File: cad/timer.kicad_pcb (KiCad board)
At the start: 2 copper layers, 47 x 47 mm, 22 parts, among them J1 Motor, J2 Pot, J4 Prog, Q1 S9012, Q2 S9013, Q3 S9012, U1 ATMEGA328P-PU, U2 LM393, U3 L293D, Y1 32.768kHz

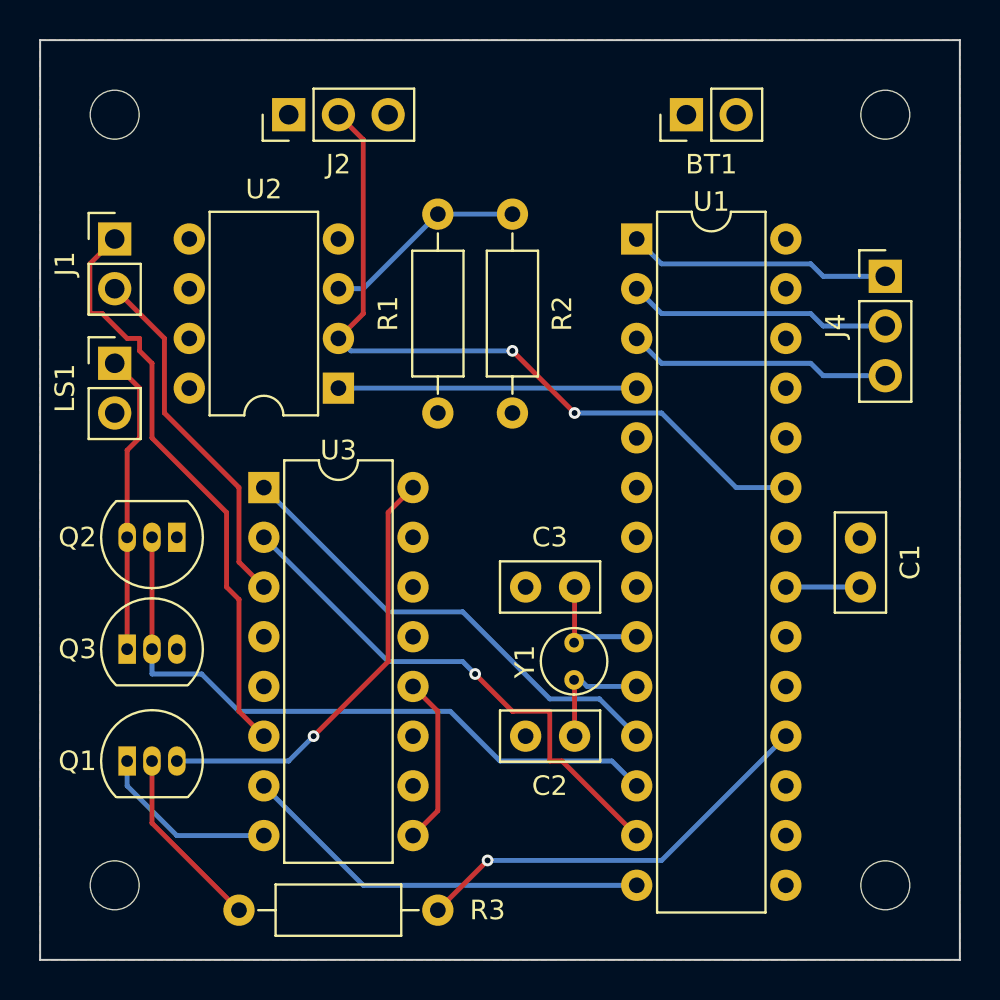
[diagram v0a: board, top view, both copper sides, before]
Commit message: Updated schematic and PCB design
- Increased hole size to 3mm
- Removed motor controller on/off switch (Q1 and R3)
- Swap transistor footprint for one that's easier to solder
- Reroute with FreeRoutingNew
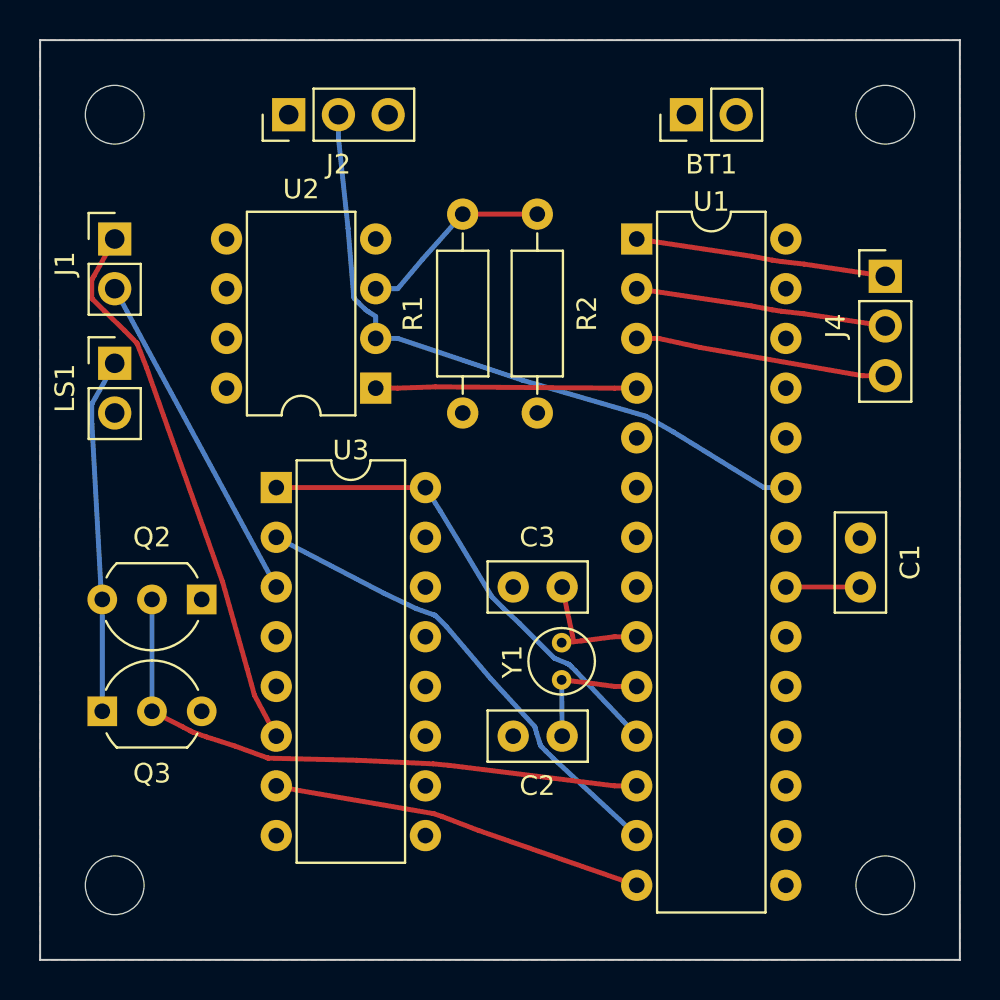
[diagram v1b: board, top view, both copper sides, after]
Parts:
- removed Q1: S9012, TO_SOT_Packages_THT:TO-92_Inline_Narrow_Oval
- removed R3: 10kΩ, Resistors_THT:R_Axial_DIN0207_L6.3mm_D2.5mm_P10.16mm_Horizontal
- H1, H2, H3, H4: value MountingHole_2.5mm -> MountingHole_3mm; footprint Mounting_Holes:MountingHole_2.5mm -> Mounting_Holes:MountingHole_3mm
- Q2, Q3: footprint TO_SOT_Packages_THT:TO-92_Inline_Narrow_Oval -> TO_SOT_Packages_THT:TO-92_Inline_Wide
- moved Q2 3.42 mm to (130.2, 97.8)
- moved Q3 3.42 mm to (125.1, 103.5)
- moved U2 1.91 mm to (139.1, 87.0)
- moved R1 1.27 mm to (143.5, 78.1)
- moved R2 1.27 mm to (147.3, 78.1)
- moved U3 0.64 mm to (134.0, 92.1)
- moved C2 0.63 mm to (148.6, 104.8)
- moved C3 0.63 mm to (148.6, 97.2)
- moved Y1 0.63 mm to (148.6, 101.9)
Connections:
- U3 pad 16: Net-(Q1-Pad3) -> Net-(U1-Pad11)
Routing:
- net Net-(Q1-Pad3): track 22.3 -> 0.00 mm, vias 1 -> 0
- net Net-(U1-Pad18): track 21.5 -> 0.00 mm, vias 1 -> 0
- net Net-(Q1-Pad2): track 9.46 -> 0.00 mm
- net VCC: track 9.31 -> 0.00 mm
- net GND: track 8.67 -> 0.00 mm
- net Net-(J2-Pad2): track 38.5 -> 34.6 mm, vias 2 -> 0
- net Net-(LS1-Pad1): track 15.4 -> 18.8 mm
- net Net-(Q2-Pad2): track 34.1 -> 31.0 mm
- net Net-(J1-Pad1): track 30.4 -> 27.9 mm
- net Net-(U1-Pad13): track 26.9 -> 24.4 mm, vias 1 -> 0
- net Net-(U1-Pad14): track 21.2 -> 19.2 mm
- net Net-(U1-Pad4): track 15.2 -> 13.3 mm
- net Net-(J1-Pad2): track 18.4 -> 17.3 mm
- net Net-(J4-Pad1): track 13.5 -> 12.8 mm
- net Net-(J4-Pad2): track 13.5 -> 12.8 mm
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
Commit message: New PCB design to match new schematic
- Isolated power networks with decoupling capacitors
- Top layer is ground, bottom layer is VCC (this seems to be the
  convention)
- Hopefully better placement of ports for external devices
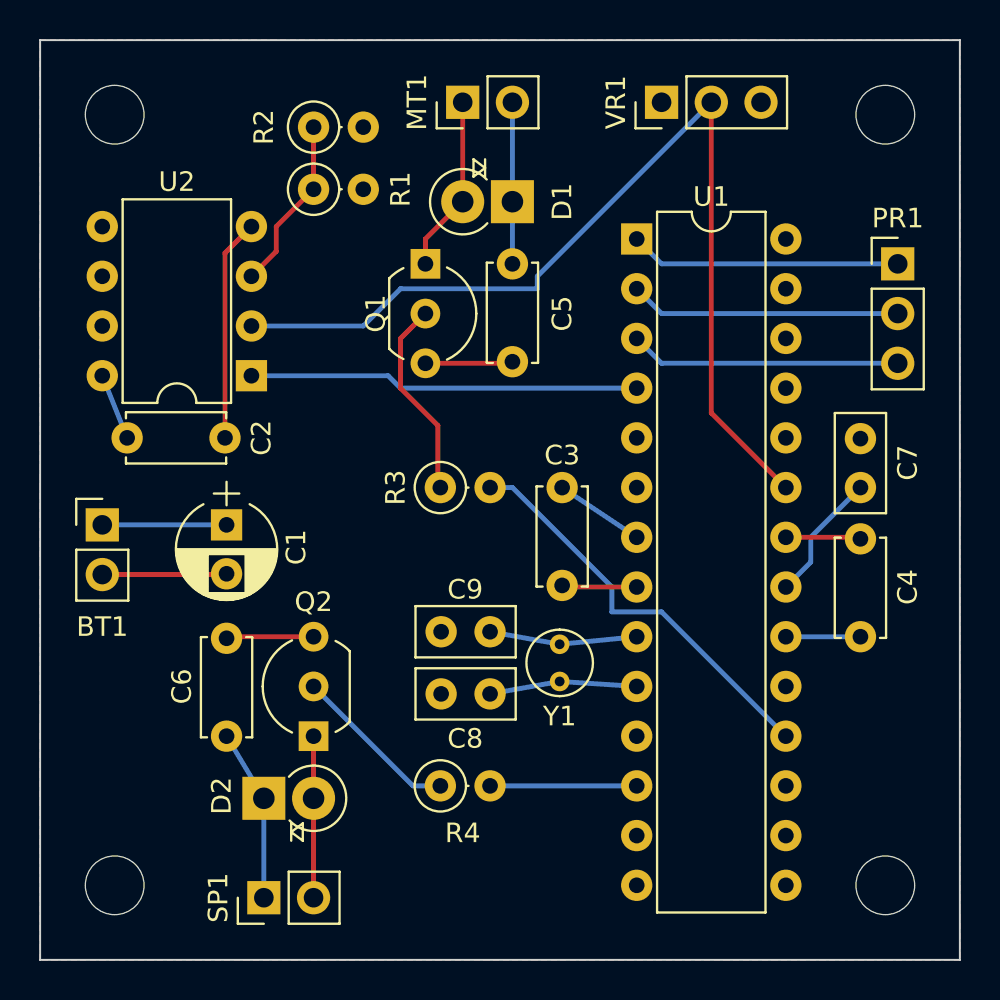
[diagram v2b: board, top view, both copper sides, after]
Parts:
- removed J1: Motor, Pin_Headers:Pin_Header_Straight_1x02_Pitch2.54mm
- removed J2: Pot, Pin_Headers:Pin_Header_Straight_1x03_Pitch2.54mm
- removed J4: Prog, Pin_Headers:Pin_Header_Straight_1x03_Pitch2.54mm
- removed LS1: Speaker, Pin_Headers:Pin_Header_Straight_1x02_Pitch2.54mm
- removed Q3: S9012, TO_SOT_Packages_THT:TO-92_Inline_Wide
- removed U3: L293D, Housings_DIP:DIP-16_W7.62mm
- added C4: 100nF, Capacitors_THT:C_Disc_D5.0mm_W2.5mm_P5.00mm, F.Cu at (163.8, 99.7)
- added C5: 100nF, Capacitors_THT:C_Disc_D5.0mm_W2.5mm_P5.00mm, F.Cu at (146.1, 80.6)
- added C6: 100nF, Capacitors_THT:C_Disc_D5.0mm_W2.5mm_P5.00mm, F.Cu at (131.4, 104.8)
- added C7: 47pF, Capacitors_THT:C_Disc_D5.0mm_W2.5mm_P2.50mm, F.Cu at (163.8, 92.1)
- added C8: 15pF, Capacitors_THT:C_Disc_D5.0mm_W2.5mm_P2.50mm, F.Cu at (144.9, 102.6)
- added C9: 15pF, Capacitors_THT:C_Disc_D5.0mm_W2.5mm_P2.50mm, F.Cu at (144.9, 99.4)
- added D1: 1N5819, Diodes_THT:D_DO-41_SOD81_P2.54mm_Vertical_KathodeUp, F.Cu at (146.1, 77.5)
- added D2: 1N5819, Diodes_THT:D_DO-41_SOD81_P2.54mm_Vertical_KathodeUp, F.Cu at (133.3, 108.0)
- added MT1: Motor, Pin_Headers:Pin_Header_Straight_1x02_Pitch2.54mm, F.Cu at (143.5, 72.4)
- added PR1: Prog, Pin_Headers:Pin_Header_Straight_1x03_Pitch2.54mm, F.Cu at (165.7, 80.6)
- added Q1: BS170, TO_SOT_Packages_THT:TO-92_Inline_Wide, F.Cu at (141.6, 80.6)
- added R3: 220Ω, Resistors_THT:R_Axial_DIN0207_L6.3mm_D2.5mm_P2.54mm_Vertical, F.Cu at (142.4, 92.1)
- added R4: 220Ω, Resistors_THT:R_Axial_DIN0207_L6.3mm_D2.5mm_P2.54mm_Vertical, F.Cu at (142.4, 107.3)
- added SP1: Speaker, Pin_Headers:Pin_Header_Straight_1x02_Pitch2.54mm, F.Cu at (133.3, 113.0)
- added VR1: Pot, Pin_Headers:Pin_Header_Straight_1x03_Pitch2.54mm, F.Cu at (153.7, 72.4)
- C1: value 47pF -> 10uF; footprint Capacitors_THT:C_Disc_D5.0mm_W2.5mm_P2.50mm -> Capacitors_THT:CP_Radial_D5.0mm_P2.50mm
- C2, C3: value 15pF -> 100nF; footprint Capacitors_THT:C_Disc_D5.0mm_W2.5mm_P2.50mm -> Capacitors_THT:C_Disc_D5.0mm_W2.5mm_P5.00mm
- Q2: value S9013 -> BS170
- R1, R2: footprint Resistors_THT:R_Axial_DIN0207_L6.3mm_D2.5mm_P10.16mm_Horizontal -> Resistors_THT:R_Axial_DIN0207_L6.3mm_D2.5mm_P2.54mm_Vertical
- moved BT1 36.5 mm to (125.1, 94.0), turned to 0 degrees
- moved C1 32.5 mm to (131.4, 94.0), turned to 270 degrees
- moved C2 26.9 mm to (126.4, 89.5), turned to 0 degrees
- moved R2 12.3 mm to (135.9, 73.7), turned to 0 degrees
- moved Q2 9.03 mm to (135.9, 104.8), turned to 90 degrees
- moved R1 7.73 mm to (135.9, 76.8), turned to 0 degrees
- moved U2 6.38 mm to (132.7, 86.4)
- moved C3 5.08 mm to (148.6, 92.1), turned to 270 degrees
- moved Y1 0.13 mm to (148.5, 102.0)
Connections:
- C1 pad 1: Net-(C1-Pad1) -> VCC
- C2 pad 1: Net-(C2-Pad1) -> VCC
- C3 pad 1: Net-(C3-Pad1) -> VCC
- Q2 pad 1: VCC -> Net-(D2-Pad2)
- Q2 pad 3: Net-(LS1-Pad1) -> GND
- U1 pad 10: Net-(C2-Pad1) -> Net-(C8-Pad1)
- U1 pad 12: Net-(Q2-Pad2) -> Net-(R4-Pad2)
- U1 pad 21: Net-(C1-Pad1) -> Net-(C7-Pad1)
- U1 pad 9: Net-(C3-Pad1) -> Net-(C9-Pad1)
- Y1 pad 1: Net-(C2-Pad1) -> Net-(C8-Pad1)
- Y1 pad 2: Net-(C3-Pad1) -> Net-(C9-Pad1)
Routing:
- net VCC: track 0.00 -> 35.2 mm
- net GND: track 0.00 -> 34.4 mm
- net Net-(J1-Pad1): track 27.9 -> 0.00 mm
- net Net-(U1-Pad11): track 24.5 -> 0.00 mm
- net Net-(U1-Pad13): track 24.4 -> 0.00 mm
- net Net-(Q2-Pad2): track 31.0 -> 8.58 mm
- net Net-(R3-Pad2): track 0.00 -> 21.1 mm
- net Net-(U1-Pad14): track 19.2 -> 0.00 mm
- net Net-(LS1-Pad1): track 18.8 -> 0.00 mm
- net Net-(J1-Pad2): track 17.3 -> 0.00 mm
- net Net-(U1-Pad23): track 34.6 -> 49.9 mm
- net Net-(Q1-Pad2): track 0.00 -> 10.3 mm
- net Net-(D1-Pad2): track 0.00 -> 9.04 mm
- net Net-(C9-Pad1): track 0.00 -> 8.41 mm
- net Net-(C8-Pad1): track 0.00 -> 8.41 mm
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- added copper zone on F.Cu, net GND
- added copper zone on B.Cu, net VCC
- removed copper zone on B.Cu, net GND
- removed copper zone on F.Cu, net VCC

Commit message: Further changes from latest KiCad version
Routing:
- net Net-(C8-Pad1): track 8.41 -> 7.56 mm
- net Net-(C9-Pad1): track 8.41 -> 7.57 mm
- net GND: track 34.4 -> 33.9 mm
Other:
- net class Default removed

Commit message: Update CAD for redesign
Also cleanup old files in cad directory
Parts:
- removed the C2 at (126.4, 89.5)
- removed the R2 at (135.9, 73.7)
- removed U2: LM393, Housings_DIP:DIP-8_W7.62mm
- added C3: 100nF, Capacitor_THT:C_Disc_D5.0mm_W2.5mm_P5.00mm, F.Cu at (152.7, 75.9)
- added D1: 1N5819, Diode_THT:D_DO-41_SOD81_P2.54mm_Vertical_KathodeUp, F.Cu at (125.7, 96.8)
- added R3: 4.7Ω, Resistor_THT:R_Axial_DIN0207_L6.3mm_D2.5mm_P2.54mm_Vertical, F.Cu at (135.4, 101.3)
- added R4: 100kΩ, Resistor_THT:R_Axial_DIN0207_L6.3mm_D2.5mm_P2.54mm_Vertical, F.Cu at (145.3, 107.4)
- BT1, MT1, SP1: footprint Pin_Headers:Pin_Header_Straight_1x02_Pitch2.54mm -> Connector_PinHeader_2.54mm:PinHeader_1x02_P2.54mm_Vertical
- C1: value 10uF -> 470µF; footprint Capacitors_THT:CP_Radial_D5.0mm_P2.50mm -> Capacitor_THT:CP_Radial_D10.0mm_P5.00mm
- C2: renamed from C5; footprint Capacitors_THT:C_Disc_D5.0mm_W2.5mm_P5.00mm -> Capacitor_THT:C_Disc_D5.0mm_W2.5mm_P5.00mm
- C4: renamed from C3; footprint Capacitors_THT:C_Disc_D5.0mm_W2.5mm_P5.00mm -> Capacitor_THT:C_Disc_D5.0mm_W2.5mm_P5.00mm
- C5: renamed from C6; footprint Capacitors_THT:C_Disc_D5.0mm_W2.5mm_P5.00mm -> Capacitor_THT:C_Disc_D5.0mm_W2.5mm_P5.00mm
- C6: renamed from C4; footprint Capacitors_THT:C_Disc_D5.0mm_W2.5mm_P5.00mm -> Capacitor_THT:C_Disc_D5.0mm_W2.5mm_P5.00mm
- C7: renamed from C9; footprint Capacitors_THT:C_Disc_D5.0mm_W2.5mm_P2.50mm -> Capacitor_THT:C_Disc_D5.0mm_W2.5mm_P2.50mm
- C8: footprint Capacitors_THT:C_Disc_D5.0mm_W2.5mm_P2.50mm -> Capacitor_THT:C_Disc_D5.0mm_W2.5mm_P2.50mm
- C9: renamed from C7; footprint Capacitors_THT:C_Disc_D5.0mm_W2.5mm_P2.50mm -> Capacitor_THT:C_Disc_D5.0mm_W2.5mm_P2.50mm
- D2: renamed from D1; footprint Diodes_THT:D_DO-41_SOD81_P2.54mm_Vertical_KathodeUp -> Diode_THT:D_DO-41_SOD81_P2.54mm_Vertical_KathodeUp
- D3: renamed from D2; footprint Diodes_THT:D_DO-41_SOD81_P2.54mm_Vertical_KathodeUp -> Diode_THT:D_DO-41_SOD81_P2.54mm_Vertical_KathodeUp
- PR1, VR1: footprint Pin_Headers:Pin_Header_Straight_1x03_Pitch2.54mm -> Connector_PinHeader_2.54mm:PinHeader_1x03_P2.54mm_Vertical
- Q1, Q2: footprint TO_SOT_Packages_THT:TO-92_Inline_Wide -> Package_TO_SOT_THT:TO-92_Inline_Wide
- R1: value 1MΩ -> 100kΩ; footprint Resistors_THT:R_Axial_DIN0207_L6.3mm_D2.5mm_P2.54mm_Vertical -> Resistor_THT:R_Axial_DIN0207_L6.3mm_D2.5mm_P2.54mm_Vertical
- R2: renamed from R3; value 220Ω -> 1kΩ; footprint Resistors_THT:R_Axial_DIN0207_L6.3mm_D2.5mm_P2.54mm_Vertical -> Resistor_THT:R_Axial_DIN0207_L6.3mm_D2.5mm_P2.54mm_Vertical
- R5: renamed from R4; value 220Ω -> 1kΩ; footprint Resistors_THT:R_Axial_DIN0207_L6.3mm_D2.5mm_P2.54mm_Vertical -> Resistor_THT:R_Axial_DIN0207_L6.3mm_D2.5mm_P2.54mm_Vertical
- U1: footprint Housings_DIP:DIP-28_W7.62mm -> Package_DIP:DIP-28_W7.62mm_Socket
- Y1: footprint Crystals:Crystal_C38-LF_d3.0mm_l8.0mm_Vertical -> Crystal:Crystal_C38-LF_D3.0mm_L8.0mm_Vertical
- moved PR1 20.4 mm to (147.1, 72.4), turned to -90 degrees
- moved C2 15.7 mm to (130.8, 77.0)
- moved D2 12.2 mm to (133.9, 77.0), turned to 0 degrees
- moved BT1 10.2 mm to (125.7, 104.1)
- moved MT1 9.65 mm to (133.9, 72.4)
- moved R2 9.00 mm to (145.3, 83.6), turned to -90 degrees
- moved R1 8.91 mm to (141.7, 83.6), turned to 90 degrees
- moved Q2 5.87 mm to (140.5, 108.5), turned to -90 degrees
- moved C9 5.18 mm to (162.3, 97.0)
- moved R5 4.70 mm to (145.3, 111.0)
- moved C1 4.56 mm to (135.9, 93.0), turned to 90 degrees
- moved Q1 2.95 mm to (138.7, 81.0), turned to 180 degrees
- moved C4 2.68 mm to (148.1, 94.7), turned to 90 degrees
- moved C6 1.53 mm to (162.3, 99.8), turned to -90 degrees
- moved C5 1.40 mm to (132.8, 104.9), turned to 0 degrees
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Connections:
- BT1 pad 1: VCC -> Net-(BT1-Pad1)
- C5 pad 1: VCC -> Net-(C5-Pad1)
- D2 pad 2: Net-(D1-Pad2) -> Net-(D2-Pad2)
- D3 pad 1: VCC -> Net-(C5-Pad1)
- MT1 pad 1: Net-(D1-Pad2) -> VCC
- MT1 pad 2: VCC -> Net-(D2-Pad2)
- Q1 pad 1: Net-(D1-Pad2) -> Net-(D2-Pad2)
- R1 pad 1: Net-(R1-Pad1) -> Net-(Q1-Pad2)
- R1 pad 2: VCC -> GND
- R2 pad 2: Net-(R3-Pad2) -> Net-(U1-Pad4)
- SP1 pad 1: VCC -> Net-(C5-Pad1)
- U1 pad 11: Net-(U1-Pad11) -> unconnected-(U1-Pad11)
- U1 pad 13: Net-(U1-Pad13) -> unconnected-(U1-Pad13)
- U1 pad 14: Net-(U1-Pad14) -> unconnected-(U1-Pad14)
- U1 pad 15: Net-(U1-Pad15) -> unconnected-(U1-Pad15)
- U1 pad 16: Net-(U1-Pad16) -> unconnected-(U1-Pad16)
- U1 pad 17: Net-(U1-Pad17) -> unconnected-(U1-Pad17)
- U1 pad 18: Net-(R3-Pad2) -> unconnected-(U1-Pad18)
- U1 pad 19: Net-(U1-Pad19) -> unconnected-(U1-Pad19)
- U1 pad 24: Net-(U1-Pad24) -> Net-(C3-Pad2)
- U1 pad 25: Net-(U1-Pad25) -> unconnected-(U1-Pad25)
- U1 pad 26: Net-(U1-Pad26) -> unconnected-(U1-Pad26)
- U1 pad 27: Net-(U1-Pad27) -> unconnected-(U1-Pad27)
- U1 pad 28: Net-(U1-Pad28) -> unconnected-(U1-Pad28)
- U1 pad 5: Net-(U1-Pad5) -> unconnected-(U1-Pad5)
- U1 pad 6: Net-(U1-Pad6) -> unconnected-(U1-Pad6)
- VR1 pad 3: GND -> Net-(C3-Pad2)
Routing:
- net VCC: track 35.2 -> 98.0 mm
- net GND: track 33.9 -> 0.00 mm
- net Net-(U1-Pad23): track 49.9 -> 21.4 mm
- net Net-(R3-Pad2): track 21.1 -> 0.00 mm
- net Net-(C3-Pad2): track 0.00 -> 17.8 mm
- net Net-(U1-Pad4): track 19.9 -> 6.52 mm
- net Net-(C5-Pad1): track 0.00 -> 11.7 mm
- net Net-(D2-Pad2): track 0.00 -> 9.58 mm
- net Net-(D1-Pad2): track 9.04 -> 0.00 mm
- net Net-(R1-Pad1): track 8.94 -> 0.00 mm
- net Net-(PR1-Pad1): track 13.9 -> 8.90 mm
- net Net-(BT1-Pad1): track 0.00 -> 4.83 mm
- net Net-(C9-Pad1): track 6.66 -> 3.05 mm
- net Net-(R5-Pad2): track 7.49 -> 5.03 mm
- net Net-(PR1-Pad3): track 13.9 -> 16.1 mm
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- added copper zone on B.Cu, net GND
- removed copper zone on F.Cu, net GND
- removed copper zone on B.Cu, net VCC
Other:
- rule pad_to_mask_clearance: 0.2 -> 0

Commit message: Label PCB
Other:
- board text added: "timer rev 2023.01 meisel.dev"
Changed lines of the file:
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@@
   )
   (gr_rect (start 121.92 69.215) (end 168.91 116.205) (layer "Edge.Cuts") (width 0.1) (fill none))
+  (gr_text "timer\nrev 2023.01\nmeisel.dev" (at 165.1 77.978 90) (layer "F.SilkS")
+    (effects (font (size 0.999998 0.999998) (thickness 0.2)) (justify right))
+  )
   (dimension (type aligned) (layer "Dwgs.User")
     (pts (xy 121.92 116.205) (xy 121.92 69.215))
